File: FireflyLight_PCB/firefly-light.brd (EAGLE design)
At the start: 47 x 17 mm, 19 parts, among them IC1 TINY85, Q1 2N7002, Q2 2N7002, Q3 2N7002

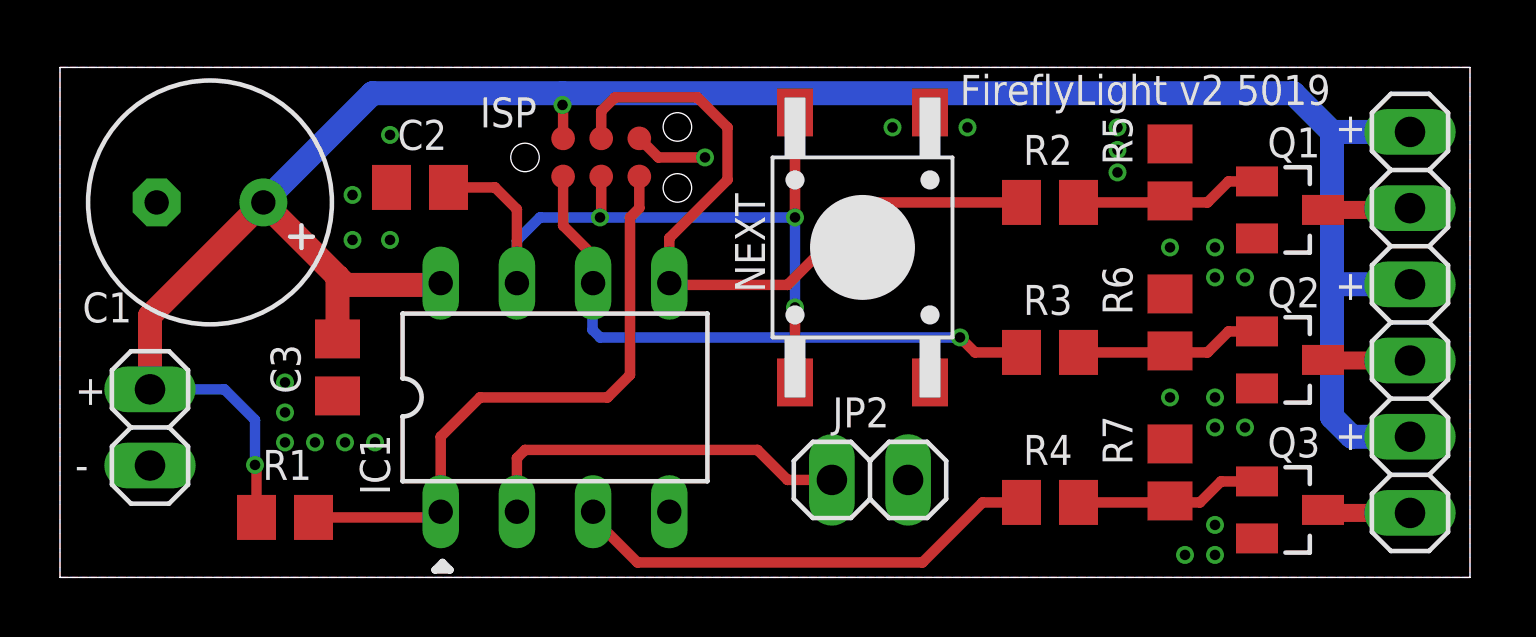
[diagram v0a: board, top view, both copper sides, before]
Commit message: attiny is now SO8
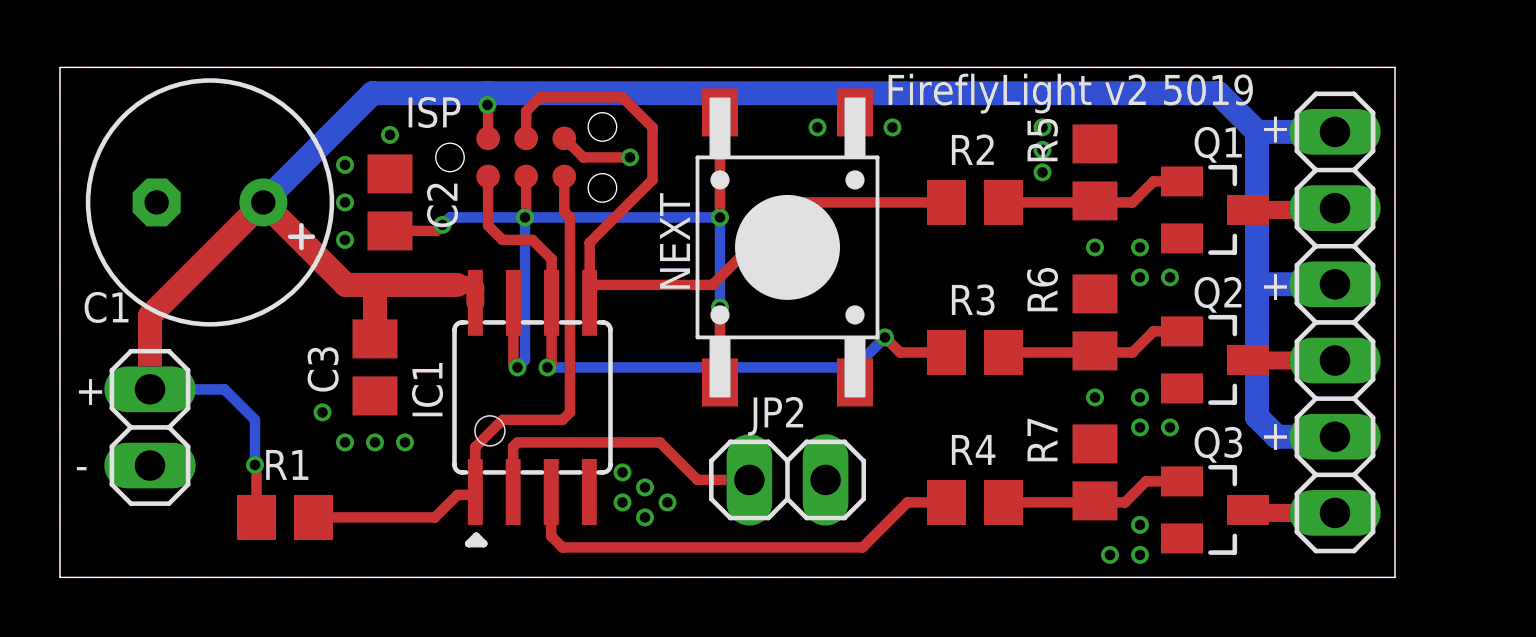
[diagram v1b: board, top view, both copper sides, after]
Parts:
- IC1: device atmel:DIL08 -> atmel:SOIC8
- moved JP2 2.75 mm to (24.2, 3.25)
- moved ISP 2.50 mm to (13.0, 14.0)
- moved JP3 2.50 mm to (42.5, 8.50)
- moved NEXT 2.50 mm to (26.5, 6.50)
- moved Q1 2.50 mm to (38.5, 12.2)
- moved Q2 2.50 mm to (38.5, 7.25)
- moved Q3 2.50 mm to (38.5, 2.25)
- moved R2 2.50 mm to (30.5, 12.5)
- moved R3 2.50 mm to (30.5, 7.50)
- moved R4 2.50 mm to (30.5, 2.50)
- moved R5 2.50 mm to (34.5, 13.5)
- moved R6 2.50 mm to (34.5, 8.50)
- moved R7 2.50 mm to (34.5, 3.50)
- moved C3 1.25 mm to (10.5, 7.00)
- moved C2 1.12 mm to (11.0, 12.5), turned to 270 degrees
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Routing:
- net N$18: track 12.8 -> 9.96 mm
- net SCK: track 26.4 -> 28.9 mm, vias 3 -> 5
- net RESET: track 20.7 -> 18.8 mm
- net MISO: track 20.1 -> 21.8 mm, vias 1 -> 2
- net VCC: track 80.9 -> 79.8 mm
- net MOSI: track 24.6 -> 25.5 mm
- net N$12: track 15.9 -> 15.4 mm
- net GND: vias 27 -> 30
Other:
- board size 47 x 17 mm -> 44.5 x 17 mm
